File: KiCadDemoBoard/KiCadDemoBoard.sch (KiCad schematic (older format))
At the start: 9 parts, among them J1 Cmd LED

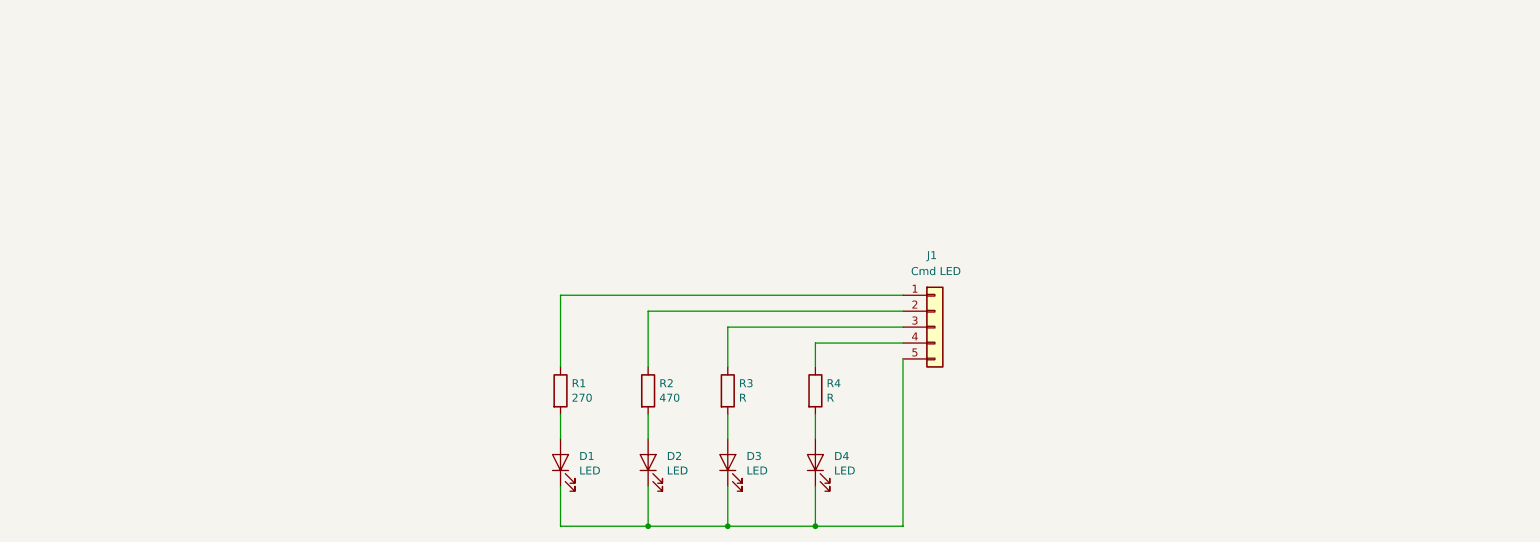
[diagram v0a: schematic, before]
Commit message: Ajout de label locaux dans le proejt KiCad
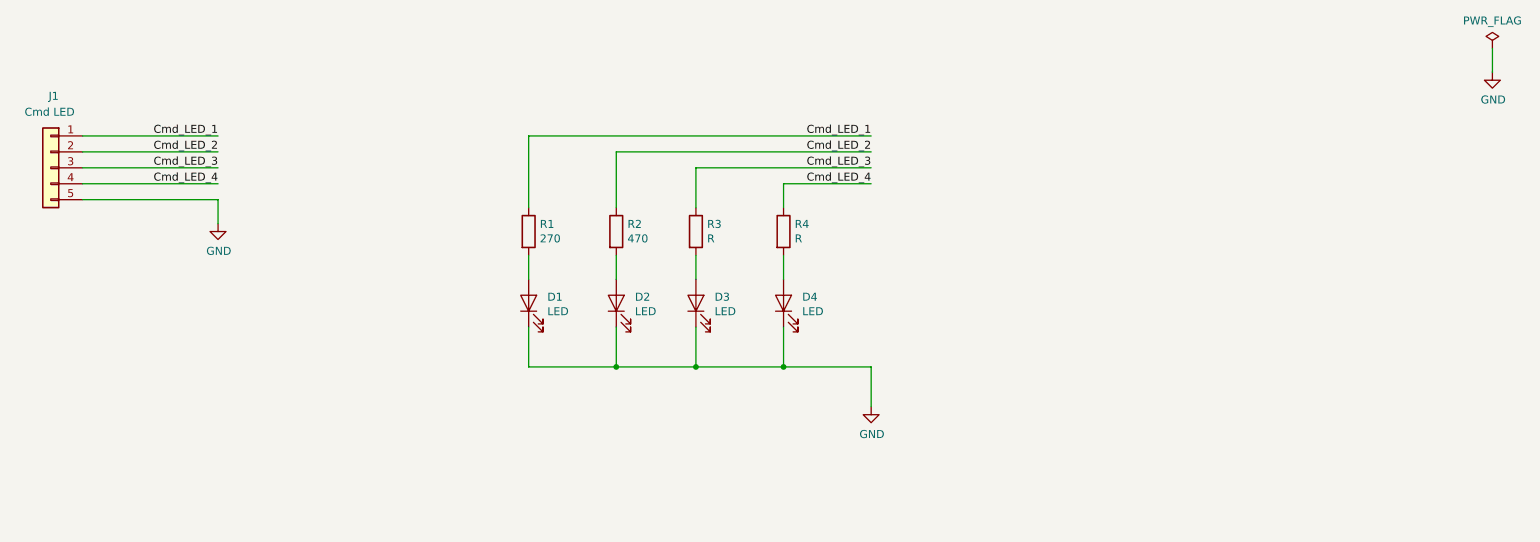
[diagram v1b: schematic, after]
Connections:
- net GND: now reaches D1.1 (K), D2.1 (K), D3.1 (K), D4.1 (K), J1.5 (Pin_5)
- net Cmd_LED_1: now reaches J1.1 (Pin_1), R1.1
- net Cmd_LED_2: now reaches J1.2 (Pin_2), R2.1
- net Cmd_LED_3: now reaches J1.3 (Pin_3), R3.1
- net Cmd_LED_4: now reaches J1.4 (Pin_4), R4.1
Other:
- moved on the sheet: D1, D2, D3, D4, J1, R1, R2, R3, R4
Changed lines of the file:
@@
 EESchema Schematic File Version 4
+LIBS:KiCadDemoBoard-cache
 EELAYER 30 0
 EELAYER END
@@
 L Device:LED D1
 U 1 1 5E203FEF
-P 4800 3650
-F 0 "D1" V 4839 3533 50  0000 R CNN
-F 1 "LED" V 4748 3533 50  0000 R CNN
-F 2 "" H 4800 3650 50  0001 C CNN
-F 3 "~" H 4800 3650 50  0001 C CNN
-	1    4800 3650
+P 4600 2650
+F 0 "D1" V 4639 2533 50  0000 R CNN
+F 1 "LED" V 4548 2533 50  0000 R CNN
+F 2 "" H 4600 2650 50  0001 C CNN
+F 3 "~" H 4600 2650 50  0001 C CNN
+	1    4600 2650
 	0    -1   -1   0
 $EndComp
@@
 L Device:R R1
 U 1 1 5E2090CF
-P 4800 3200
-F 0 "R1" H 4870 3246 50  0000 L CNN
-F 1 "270" H 4870 3155 50  0000 L CNN
-F 2 "" V 4730 3200 50  0001 C CNN
-F 3 "~" H 4800 3200 50  0001 C CNN
-	1    4800 3200
+P 4600 2200
+F 0 "R1" H 4670 2246 50  0000 L CNN
+F 1 "270" H 4670 2155 50  0000 L CNN
+F 2 "" V 4530 2200 50  0001 C CNN
+F 3 "~" H 4600 2200 50  0001 C CNN
+	1    4600 2200
 	1    0    0    -1
 $EndComp
@@
 L Connector_Generic:Conn_01x05 J1
 U 1 1 5E20B761
-P 7150 2800
-F 0 "J1" H 7100 3250 50  0000 L CNN
-F 1 "Cmd LED" H 7000 3150 50  0000 L CNN
-F 2 "" H 7150 2800 50  0001 C CNN
-F 3 "~" H 7150 2800 50  0001 C CNN
-	1    7150 2800
-	1    0    0    -1
-$EndComp
-Wire Wire Line
-	4800 3800 4800 4050
-Wire Wire Line
-	4800 4050 5350 4050
-Wire Wire Line
-	6950 4050 6950 3000
-Wire Wire Line
-	4800 3050 4800 2600
-Wire Wire Line
-	4800 3350 4800 3500
+P 1600 1800
+F 0 "J1" H 1550 2250 50  0000 L CNN
+F 1 "Cmd LED" H 1450 2150 50  0000 L CNN
+F 2 "" H 1600 1800 50  0001 C CNN
+F 3 "~" H 1600 1800 50  0001 C CNN
+	1    1600 1800
+	-1   0    0    -1
+$EndComp
+Wire Wire Line
+	4600 2800 4600 3050
+Wire Wire Line
+	4600 3050 5150 3050
+Wire Wire Line
+	4600 2050 4600 1600
+Wire Wire Line
+	4600 2350 4600 2500
 $Comp
 L Device:LED D2
 U 1 1 5E226705
-P 5350 3650
-F 0 "D2" V 5389 3533 50  0000 R CNN
-F 1 "LED" V 5298 3533 50  0000 R CNN
-F 2 "" H 5350 3650 50  0001 C CNN
-F 3 "~" H 5350 3650 50  0001 C CNN
-	1    5350 3650
+P 5150 2650
+F 0 "D2" V 5189 2533 50  0000 R CNN
+F 1 "LED" V 5098 2533 50  0000 R CNN
+F 2 "" H 5150 2650 50  0001 C CNN
+F 3 "~" H 5150 2650 50  0001 C CNN
+	1    5150 2650
 	0    -1   -1   0
 $EndComp
@@
 L Device:R R2
 U 1 1 5E22670F
-P 5350 3200
-F 0 "R2" H 5420 3246 50  0000 L CNN
-F 1 "470" H 5420 3155 50  0000 L CNN
-F 2 "" V 5280 3200 50  0001 C CNN
-F 3 "~" H 5350 3200 50  0001 C CNN
-	1    5350 3200
-	1    0    0    -1
-$EndComp
-Wire Wire Line
-	5350 3800 5350 4050
-Wire Wire Line
-	5350 3350 5350 3500
-Connection ~ 5350 4050
-Wire Wire Line
-	5350 4050 5850 4050
+P 5150 2200
+F 0 "R2" H 5220 2246 50  0000 L CNN
+F 1 "470" H 5220 2155 50  0000 L CNN
+F 2 "" V 5080 2200 50  0001 C CNN
+F 3 "~" H 5150 2200 50  0001 C CNN
+	1    5150 2200
+	1    0    0    -1
+$EndComp
+Wire Wire Line
+	5150 2800 5150 3050
+Wire Wire Line
+	5150 2350 5150 2500
+Connection ~ 5150 3050
+Wire Wire Line
+	5150 3050 5650 3050
 $Comp
 L Device:LED D3
 U 1 1 5E22BD71
-P 5850 3650
-F 0 "D3" V 5889 3533 50  0000 R CNN
-F 1 "LED" V 5798 3533 50  0000 R CNN
-F 2 "" H 5850 3650 50  0001 C CNN
-F 3 "~" H 5850 3650 50  0001 C CNN
-	1    5850 3650
+P 5650 2650
+F 0 "D3" V 5689 2533 50  0000 R CNN
+F 1 "LED" V 5598 2533 50  0000 R CNN
+F 2 "" H 5650 2650 50  0001 C CNN
+F 3 "~" H 5650 2650 50  0001 C CNN
+	1    5650 2650
 	0    -1   -1   0
 $EndComp
@@
 L Device:R R3
 U 1 1 5E22BD7B
-P 5850 3200
-F 0 "R3" H 5920 3246 50  0000 L CNN
-F 1 "R" H 5920 3155 50  0000 L CNN
-F 2 "" V 5780 3200 50  0001 C CNN
-F 3 "~" H 5850 3200 50  0001 C CNN
-	1    5850 3200
-	1    0    0    -1
-$EndComp
-Wire Wire Line
-	5850 3800 5850 4050
-Wire Wire Line
-	5850 3350 5850 3500
+P 5650 2200
+F 0 "R3" H 5720 2246 50  0000 L CNN
+F 1 "R" H 5720 2155 50  0000 L CNN
+F 2 "" V 5580 2200 50  0001 C CNN
+F 3 "~" H 5650 2200 50  0001 C CNN
+	1    5650 2200
+	1    0    0    -1
+$EndComp
+Wire Wire Line
+	5650 2800 5650 3050
+Wire Wire Line
+	5650 2350 5650 2500
 $Comp
 L Device:LED D4
 U 1 1 5E22BD88
-P 6400 3650
-F 0 "D4" V 6439 3533 50  0000 R CNN
-F 1 "LED" V 6348 3533 50  0000 R CNN
-F 2 "" H 6400 3650 50  0001 C CNN
-F 3 "~" H 6400 3650 50  0001 C CNN
-	1    6400 3650
+P 6200 2650
+F 0 "D4" V 6239 2533 50  0000 R CNN
+F 1 "LED" V 6148 2533 50  0000 R CNN
+F 2 "" H 6200 2650 50  0001 C CNN
+F 3 "~" H 6200 2650 50  0001 C CNN
+	1    6200 2650
 	0    -1   -1   0
 $EndComp
@@
 L Device:R R4
 U 1 1 5E22BD92
-P 6400 3200
-F 0 "R4" H 6470 3246 50  0000 L CNN
-F 1 "R" H 6470 3155 50  0000 L CNN
-F 2 "" V 6330 3200 50  0001 C CNN
-F 3 "~" H 6400 3200 50  0001 C CNN
-	1    6400 3200
-	1    0    0    -1
-$EndComp
-Wire Wire Line
-	6400 3800 6400 4050
-Wire Wire Line
-	6400 3350 6400 3500
-Connection ~ 5850 4050
-Wire Wire Line
-	5850 4050 6400 4050
-Connection ~ 6400 4050
-Wire Wire Line
-	6400 4050 6950 4050
-Wire Wire Line
-	4800 2600 6950 2600
-Wire Wire Line
-	6950 2800 5850 2800
-Wire Wire Line
-	5850 2800 5850 3050
-Wire Wire Line
-	6950 2700 5350 2700
-Wire Wire Line
-	5350 2700 5350 3050
-Wire Wire Line
-	6400 3050 6400 2900
-Wire Wire Line
-	6400 2900 6950 2900
+P 6200 2200
+F 0 "R4" H 6270 2246 50  0000 L CNN
+F 1 "R" H 6270 2155 50  0000 L CNN
+F 2 "" V 6130 2200 50  0001 C CNN
+F 3 "~" H 6200 2200 50  0001 C CNN
+	1    6200 2200
+	1    0    0    -1
+$EndComp
+Wire Wire Line
+	6200 2800 6200 3050
+Wire Wire Line
+	6200 2350 6200 2500
+Connection ~ 5650 3050
+Wire Wire Line
+	5650 3050 6200 3050
+Connection ~ 6200 3050
+Wire Wire Line
+	6200 3050 6750 3050
+Wire Wire Line
+	4600 1600 6750 1600
+Wire Wire Line
+	6750 1800 5650 1800
+Wire Wire Line
+	5650 1800 5650 2050
+Wire Wire Line
+	6750 1700 5150 1700
+Wire Wire Line
+	5150 1700 5150 2050
+Wire Wire Line
+	6200 2050 6200 1900
+Wire Wire Line
+	6200 1900 6750 1900
+Text Label 6750 1600 2    50   ~ 0
+Cmd_LED_1
+Text Label 6750 1700 2    50   ~ 0
+Cmd_LED_2
+Text Label 6750 1800 2    50   ~ 0
+Cmd_LED_3
+Text Label 6750 1900 2    50   ~ 0
+Cmd_LED_4
+Wire Wire Line
+	1800 1600 2650 1600
+Wire Wire Line
+	1800 1700 2650 1700
+Wire Wire Line
+	1800 1800 2650 1800
+Wire Wire Line
+	1800 1900 2650 1900
+Wire Wire Line
+	1800 2000 2650 2000
+Wire Wire Line
+	2650 2000 2650 2150
+Text Label 2650 1600 2    50   ~ 0
+Cmd_LED_1
+Text Label 2650 1700 2    50   ~ 0
+Cmd_LED_2
+Text Label 2650 1800 2    50   ~ 0
+Cmd_LED_3
+Text Label 2650 1900 2    50   ~ 0
+Cmd_LED_4
+$Comp
+L power:GND #PWR0101
+U 1 1 5E21115A
+P 6750 3300
+F 0 "#PWR0101" H 6750 3050 50  0001 C CNN
+F 1 "GND" H 6755 3127 50  0000 C CNN
+F 2 "" H 6750 3300 50  0001 C CNN
+F 3 "" H 6750 3300 50  0001 C CNN
+	1    6750 3300
+	1    0    0    -1
+$EndComp
+Wire Wire Line
+	6750 3050 6750 3300
+$Comp
+L power:GND #PWR0102
+U 1 1 5E2128C5
+P 2650 2150
+F 0 "#PWR0102" H 2650 1900 50  0001 C CNN
+F 1 "GND" H 2655 1977 50  0000 C CNN
+F 2 "" H 2650 2150 50  0001 C CNN
+F 3 "" H 2650 2150 50  0001 C CNN
+	1    2650 2150
+	1    0    0    -1
+$EndComp
+$Comp
+L power:GND #PWR0103
+U 1 1 5E21407A
+P 10650 1200
+F 0 "#PWR0103" H 10650 950 50  0001 C CNN
+F 1 "GND" H 10655 1027 50  0000 C CNN
+F 2 "" H 10650 1200 50  0001 C CNN
+F 3 "" H 10650 1200 50  0001 C CNN
+	1    10650 1200
+	1    0    0    -1
+$EndComp
+$Comp
+L power:PWR_FLAG #FLG0101
+U 1 1 5E215858
+P 10650 1050
+F 0 "#FLG0101" H 10650 1125 50  0001 C CNN
+F 1 "PWR_FLAG" H 10650 1223 50  0000 C CNN
+F 2 "" H 10650 1050 50  0001 C CNN
+F 3 "~" H 10650 1050 50  0001 C CNN
+	1    10650 1050
+	1    0    0    -1
+$EndComp
+Wire Wire Line
+	10650 1050 10650 1200
 $EndSCHEMATC
